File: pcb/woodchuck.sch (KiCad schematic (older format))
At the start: 5 parts, among them IC101 ADP3335, P101 CONN_01X02

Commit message: Ran ERC and regenerated netlist
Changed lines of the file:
@@
 Wire Notes Line
 	6450 5900 3850 5900
-Wire Wire Line
-	4200 6550 4850 6550
 Wire Notes Line
 	3850 5900 3850 7250
@@
 	5550 6550 6100 6550
 Wire Wire Line
-	4750 6650 4850 6650
-Wire Wire Line
 	4750 6450 4750 6650
 Connection ~ 4750 6550
@@
 Wire Wire Line
 	4200 6650 4200 6550
-Wire Wire Line
-	4750 6450 4850 6450
 Connection ~ 4200 6850
 Connection ~ 4400 6850
@@
 Text Label 6450 2200 0    60   ~ 0
 MTX2_P1
+Wire Wire Line
+	4850 6450 4750 6450
+Wire Wire Line
+	4200 6550 4850 6550
+Wire Wire Line
+	4750 6650 4850 6650
 $EndSCHEMATC

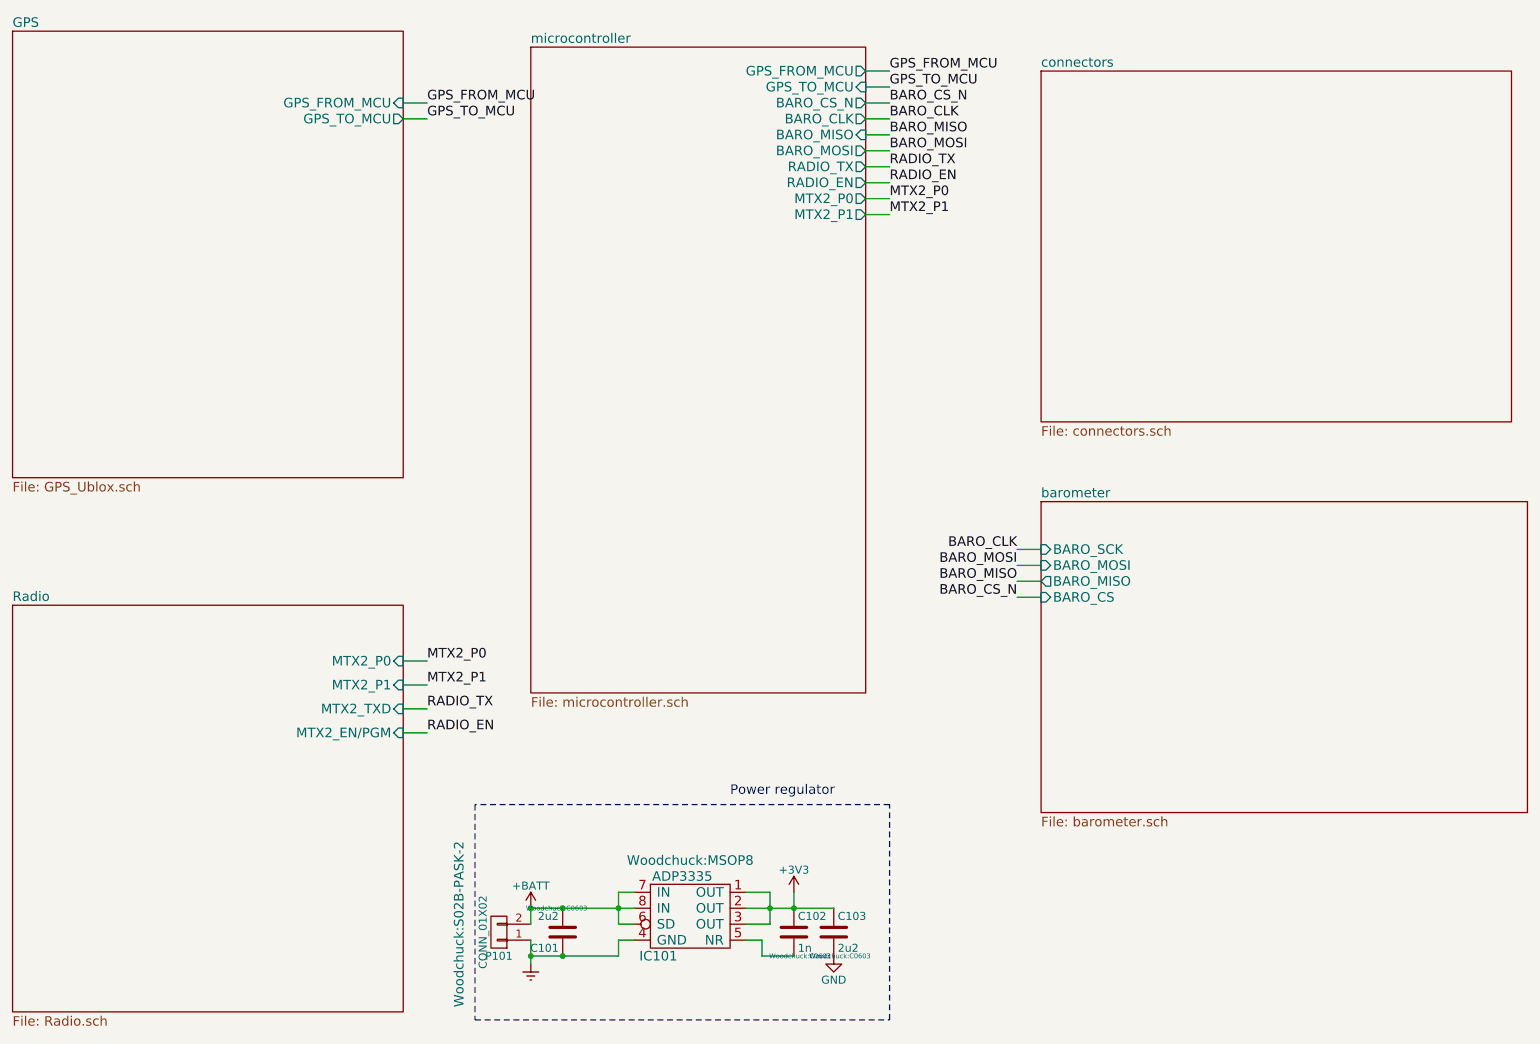
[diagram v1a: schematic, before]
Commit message: Fixed some errors in the schematics
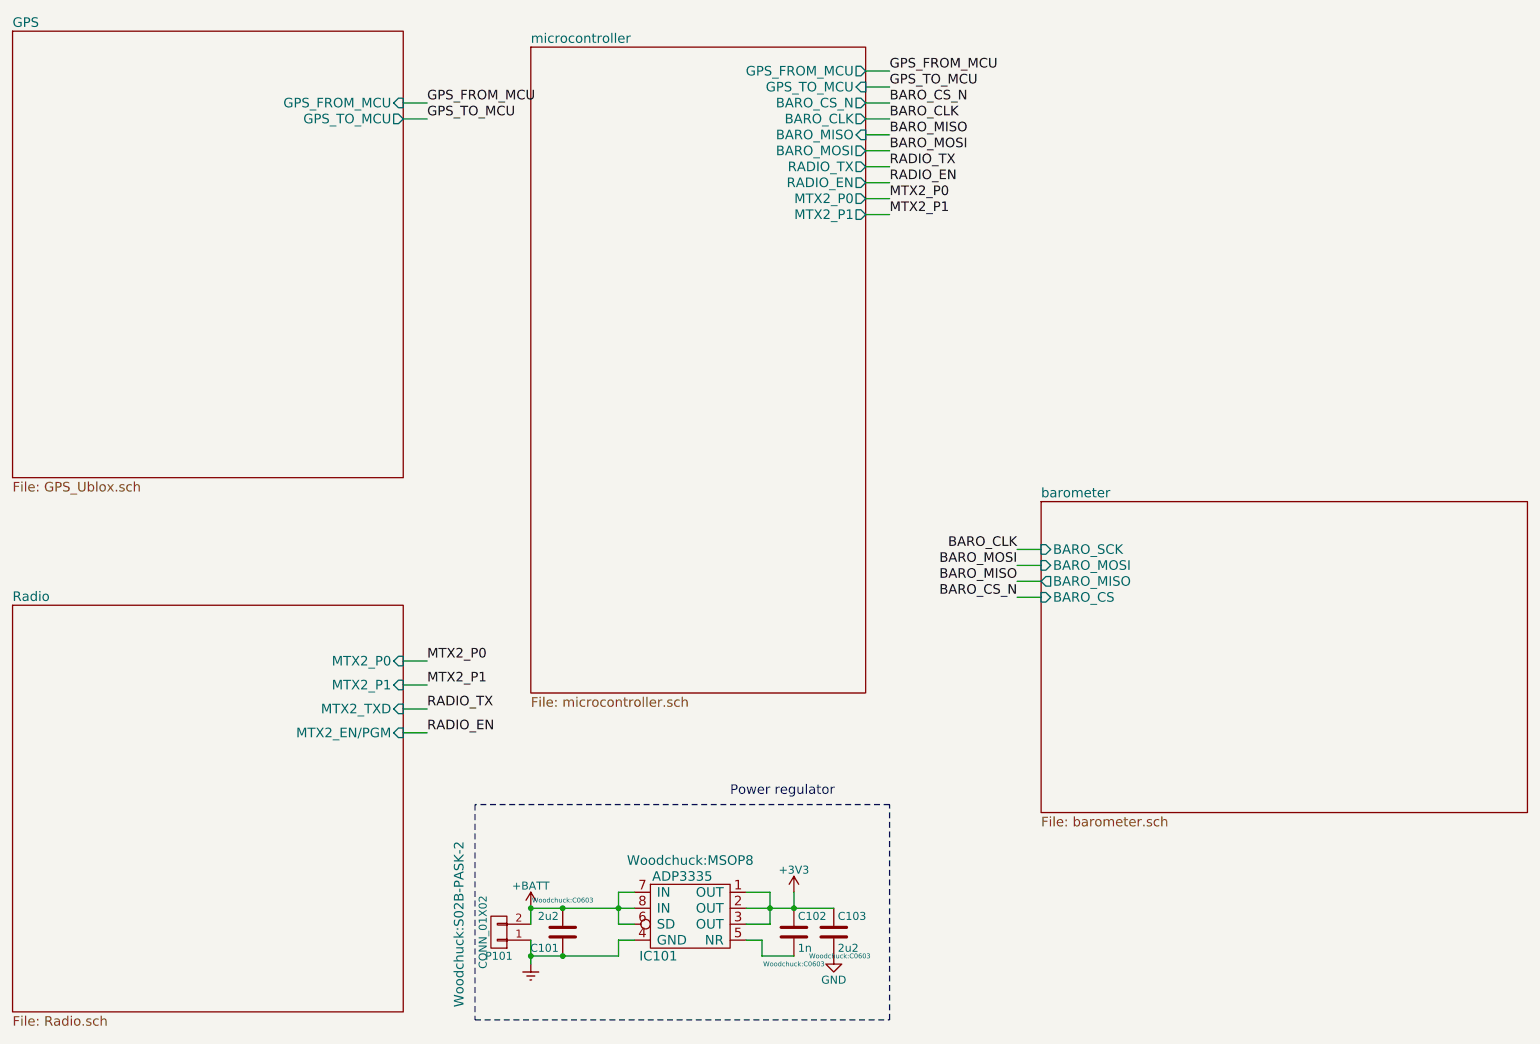
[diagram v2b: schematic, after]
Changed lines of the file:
@@
 $Descr A4 11693 8268
 encoding utf-8
-Sheet 1 6
+Sheet 1 5
 Title ""
 Date ""
@@
 $EndSheet
 $Sheet
-S 7400 1300 2950 2200
-U 5657409B
-F0 "connectors" 60
-F1 "connectors.sch" 60
-$EndSheet
-$Sheet
 S 7400 4000 3050 1950
 U 5657409E
@@
 F 0 "C102" H 5875 6800 50  0000 L CNN
 F 1 "1n" H 5875 6600 50  0000 L CNN
-F 2 "Woodchuck:C0603" H 5888 6550 30  0000 C CNN
+F 2 "Woodchuck:C0603" H 5850 6500 30  0000 C CNN
 F 3 "" H 5850 6700 60  0000 C CNN
 F 4 "Value" H 5850 6700 60  0001 C CNN "Digikey"
@@
 F 0 "C101" H 4425 6800 50  0000 L CNN
 F 1 "2u2" H 4425 6600 50  0000 L CNN
-F 2 "Woodchuck:C0603" H 4438 6550 30  0000 C CNN
+F 2 "Woodchuck:C0603" H 4400 6500 30  0000 C CNN
 F 3 "" H 4400 6700 60  0000 C CNN
 F 4 "Value" H 4400 6700 60  0001 C CNN "Digikey"

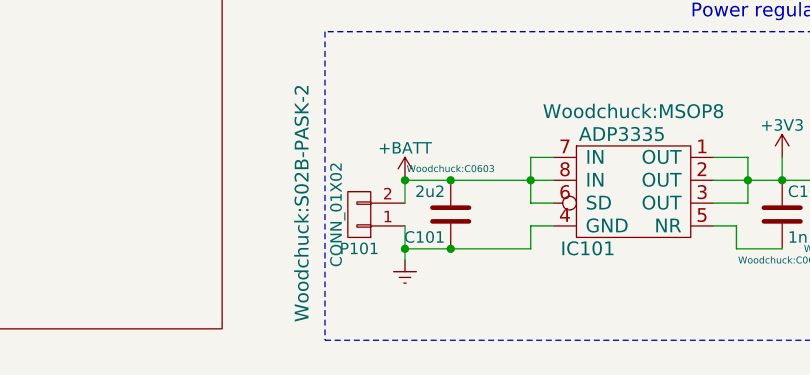
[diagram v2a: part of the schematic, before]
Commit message: Worked on PCB layout
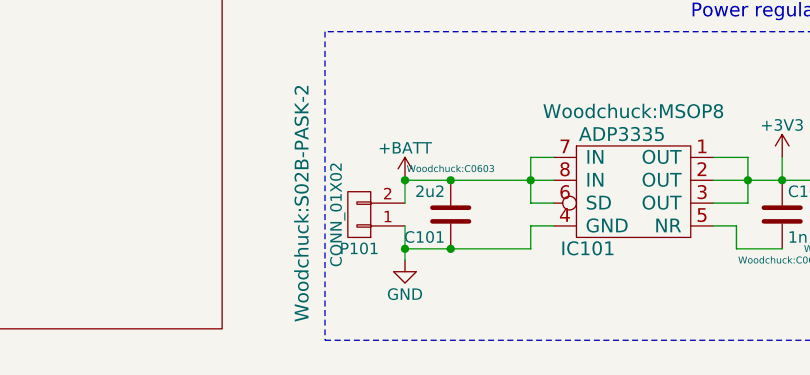
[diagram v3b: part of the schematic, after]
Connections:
- net Earth is gone; now on net GND: C101.1, IC101.4 (GND), P101.1 (P1)
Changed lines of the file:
@@
-$EndComp
-$Comp
-L Earth #PWR01
-U 1 1 565E4C8C
-P 4200 6900
-F 0 "#PWR01" H 4200 6650 50  0001 C CNN
-F 1 "Earth" H 4200 6750 50  0001 C CNN
-F 2 "" H 4200 6900 60  0000 C CNN
-F 3 "" H 4200 6900 60  0000 C CNN
-	1    4200 6900
-	1    0    0    -1
 $EndComp
 $Comp
@@
 $EndComp
 $Comp
-L GND #PWR02
+L GND #PWR01
 U 1 1 565E565A
 P 6100 6850
-F 0 "#PWR02" H 6100 6600 50  0001 C CNN
+F 0 "#PWR01" H 6100 6600 50  0001 C CNN
 F 1 "GND" H 6100 6700 50  0000 C CNN
 F 2 "" H 6100 6850 60  0000 C CNN
@@
 $EndComp
 $Comp
-L +BATT #PWR03
+L +BATT #PWR02
 U 1 1 565EBEEE
 P 4200 6550
-F 0 "#PWR03" H 4200 6400 50  0001 C CNN
+F 0 "#PWR02" H 4200 6400 50  0001 C CNN
 F 1 "+BATT" H 4200 6690 50  0000 C CNN
 F 2 "" H 4200 6550 60  0000 C CNN
@@
 $EndComp
 $Comp
-L +3V3 #PWR04
+L +3V3 #PWR03
 U 1 1 565EC163
 P 5850 6450
-F 0 "#PWR04" H 5850 6300 50  0001 C CNN
+F 0 "#PWR03" H 5850 6300 50  0001 C CNN
 F 1 "+3V3" H 5850 6590 50  0000 C CNN
 F 2 "" H 5850 6450 60  0000 C CNN
@@
 Wire Wire Line
 	4750 6650 4850 6650
+$Comp
+L GND #PWR04
+U 1 1 56C23CD2
+P 4200 6900
+F 0 "#PWR04" H 4200 6650 50  0001 C CNN
+F 1 "GND" H 4200 6750 50  0000 C CNN
+F 2 "" H 4200 6900 50  0000 C CNN
+F 3 "" H 4200 6900 50  0000 C CNN
+	1    4200 6900
+	1    0    0    -1
+$EndComp
 $EndSCHEMATC

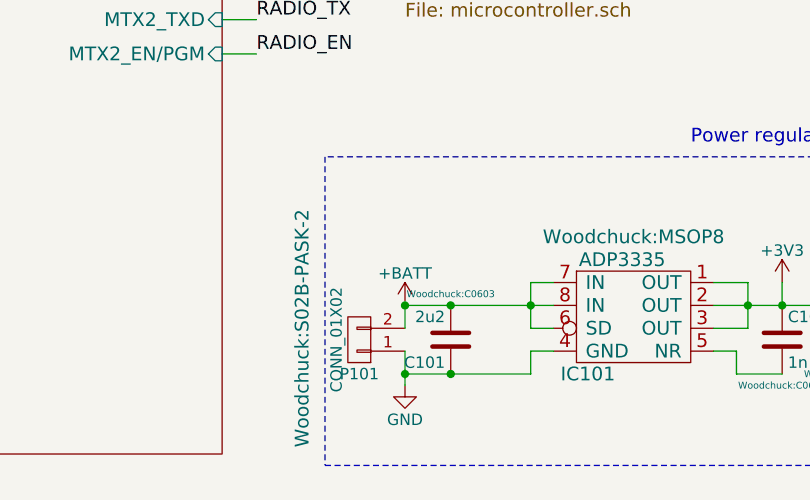
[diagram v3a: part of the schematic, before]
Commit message: Continued routing PCB, changed order of LEDs
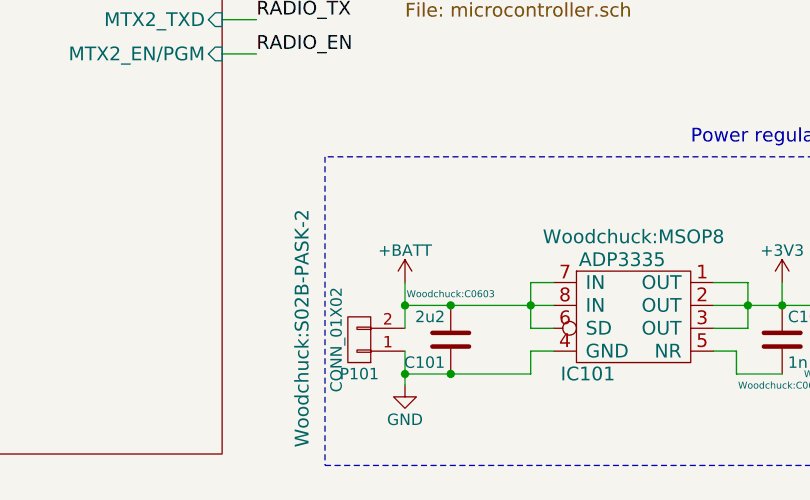
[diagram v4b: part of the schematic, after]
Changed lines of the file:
@@
 L +BATT #PWR02
 U 1 1 565EBEEE
-P 4200 6550
-F 0 "#PWR02" H 4200 6400 50  0001 C CNN
-F 1 "+BATT" H 4200 6690 50  0000 C CNN
-F 2 "" H 4200 6550 60  0000 C CNN
-F 3 "" H 4200 6550 60  0000 C CNN
-	1    4200 6550
+P 4200 6450
+F 0 "#PWR02" H 4200 6300 50  0001 C CNN
+F 1 "+BATT" H 4200 6590 50  0000 C CNN
+F 2 "" H 4200 6450 60  0000 C CNN
+F 3 "" H 4200 6450 60  0000 C CNN
+	1    4200 6450
 	1    0    0    -1
 $EndComp
@@
 	3850 5900 3850 7250
 Wire Wire Line
-	5550 6450 5700 6450
-Wire Wire Line
 	5700 6450 5700 6650
 Wire Wire Line
@@
 	4200 6750 4200 6900
 Wire Wire Line
-	4200 6650 4200 6550
+	4200 6450 4200 6650
 Connection ~ 4200 6850
 Connection ~ 4400 6850
@@
 	1    0    0    -1
 $EndComp
+Wire Wire Line
+	5550 6450 5700 6450
 $EndSCHEMATC

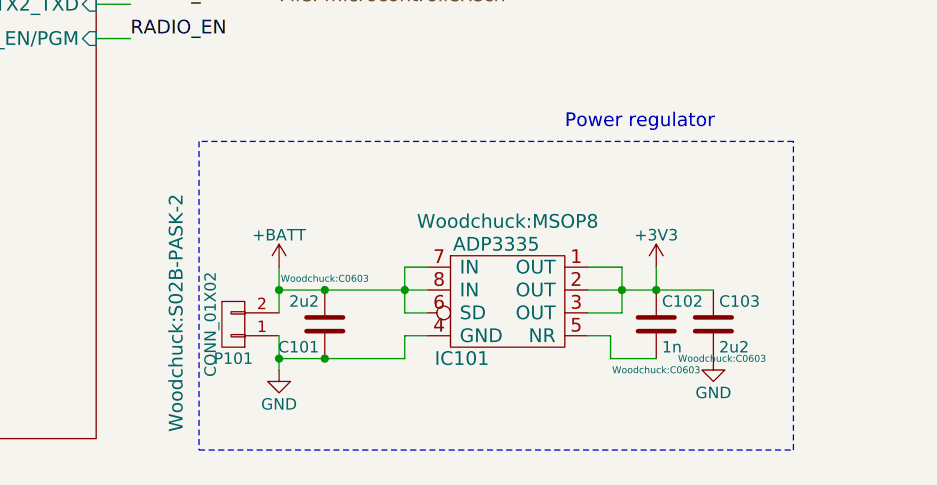
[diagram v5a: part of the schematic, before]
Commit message: Hide footprints on schematic, fix overlaps
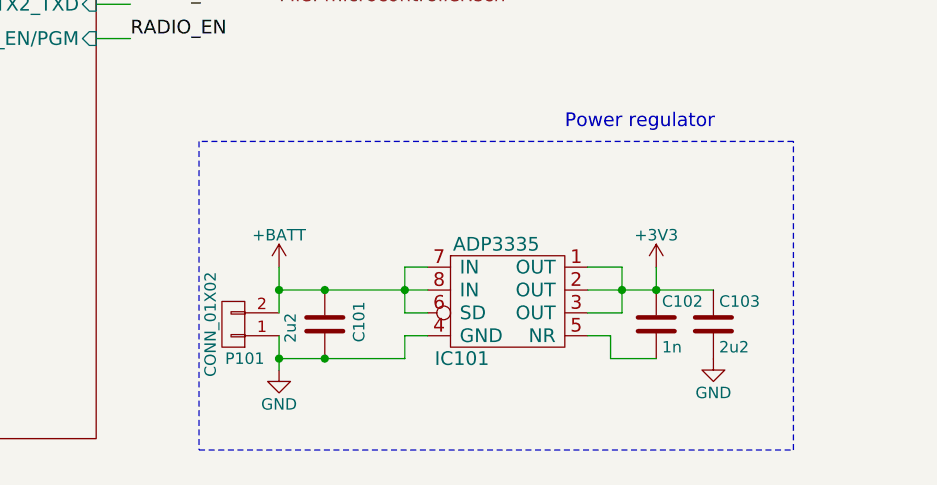
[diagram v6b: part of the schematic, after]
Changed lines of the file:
@@
 F 0 "IC101" H 5000 6250 60  0000 C CNN
 F 1 "ADP3335" H 5150 6750 60  0000 C CNN
-F 2 "Woodchuck:MSOP8" H 5200 6850 60  0000 C CNN
+F 2 "Woodchuck:MSOP8" H 5200 6850 60  0001 C CNN
 F 3 "" H 5600 6150 60  0000 C CNN
 F 4 "Value" H 5200 6550 60  0001 C CNN "Digikey"
@@
 F 0 "C102" H 5875 6800 50  0000 L CNN
 F 1 "1n" H 5875 6600 50  0000 L CNN
-F 2 "Woodchuck:C0603" H 5850 6500 30  0000 C CNN
+F 2 "Woodchuck:C0603" H 5850 6500 30  0001 C CNN
 F 3 "" H 5850 6700 60  0000 C CNN
 F 4 "Value" H 5850 6700 60  0001 C CNN "Digikey"
@@
 F 0 "C103" H 6125 6800 50  0000 L CNN
 F 1 "2u2" H 6125 6600 50  0000 L CNN
-F 2 "Woodchuck:C0603" H 6138 6550 30  0000 C CNN
+F 2 "Woodchuck:C0603" H 6138 6550 30  0001 C CNN
 F 3 "" H 6100 6700 60  0000 C CNN
 F 4 "Value" H 6100 6700 60  0001 C CNN "Digikey"
@@
 U 1 1 565E43E2
 P 4400 6700
-F 0 "C101" H 4425 6800 50  0000 L CNN
-F 1 "2u2" H 4425 6600 50  0000 L CNN
-F 2 "Woodchuck:C0603" H 4400 6500 30  0000 C CNN
+F 0 "C101" V 4250 6600 50  0000 L CNN
+F 1 "2u2" V 4550 6650 50  0000 L CNN
+F 2 "Woodchuck:C0603" H 4400 6500 30  0001 C CNN
 F 3 "" H 4400 6700 60  0000 C CNN
 F 4 "Value" H 4400 6700 60  0001 C CNN "Digikey"
@@
 U 1 1 565EBDD9
 P 4000 6700
-F 0 "P101" H 4000 6850 50  0000 C CNN
+F 0 "P101" H 3950 6850 50  0000 C CNN
 F 1 "CONN_01X02" V 4100 6700 50  0000 C CNN
-F 2 "Woodchuck:S02B-PASK-2" V 4250 6650 60  0000 C CNN
+F 2 "Woodchuck:S02B-PASK-2" V 4250 6650 60  0001 C CNN
 F 3 "" H 4000 6700 60  0000 C CNN
 F 4 "Value" H 4000 6700 60  0001 C CNN "Digikey"

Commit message: last commit before reloading net list
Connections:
- net +BATT: now also P101.1 (P1); no longer P101.2 (P2)
- net GND: now also P101.2 (P2); no longer P101.1 (P1)
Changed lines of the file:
@@
 $EndComp
 $Comp
-L GND #PWR104
+L GND #PWR01
 U 1 1 565E565A
 P 6100 6850
-F 0 "#PWR104" H 6100 6600 50  0001 C CNN
+F 0 "#PWR01" H 6100 6600 50  0001 C CNN
 F 1 "GND" H 6100 6700 50  0000 C CNN
 F 2 "" H 6100 6850 60  0000 C CNN
@@
 F 6 "Value" H 4000 6700 60  0001 C CNN "Fieldname"
 	1    4000 6700
-	-1   0    0    1
+	-1   0    0    -1
 $EndComp
 $Comp
-L +BATT #PWR101
+L +BATT #PWR02
 U 1 1 565EBEEE
 P 4200 6450
-F 0 "#PWR101" H 4200 6300 50  0001 C CNN
+F 0 "#PWR02" H 4200 6300 50  0001 C CNN
 F 1 "+BATT" H 4200 6590 50  0000 C CNN
 F 2 "" H 4200 6450 60  0000 C CNN
@@
 $EndComp
 $Comp
-L +3V3 #PWR103
+L +3V3 #PWR03
 U 1 1 565EC163
 P 5850 6450
-F 0 "#PWR103" H 5850 6300 50  0001 C CNN
+F 0 "#PWR03" H 5850 6300 50  0001 C CNN
 F 1 "+3V3" H 5850 6590 50  0000 C CNN
 F 2 "" H 5850 6450 60  0000 C CNN
@@
 	4750 6650 4850 6650
 $Comp
-L GND #PWR102
+L GND #PWR04
 U 1 1 56C23CD2
 P 4200 6900
-F 0 "#PWR102" H 4200 6650 50  0001 C CNN
+F 0 "#PWR04" H 4200 6650 50  0001 C CNN
 F 1 "GND" H 4200 6750 50  0000 C CNN
 F 2 "" H 4200 6900 50  0000 C CNN

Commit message: Generated gerbers, DONE!
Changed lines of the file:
@@
 Wire Wire Line
 	5550 6450 5700 6450
+$Comp
+L PWR #FLG05
+U 1 1 56E22CC5
+P 4400 6550
+F 0 "#FLG05" H 4400 6710 50  0001 C CNN
+F 1 "PWR" H 4400 6640 50  0000 C CNN
+F 2 "" H 4400 6550 50  0001 C CNN
+F 3 "" H 4400 6550 50  0001 C CNN
+	1    4400 6550
+	1    0    0    -1
+$EndComp
 $EndSCHEMATC
